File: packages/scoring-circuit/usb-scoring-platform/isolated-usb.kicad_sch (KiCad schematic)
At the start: 10 parts, among them U18 ADuM3160BRWZ

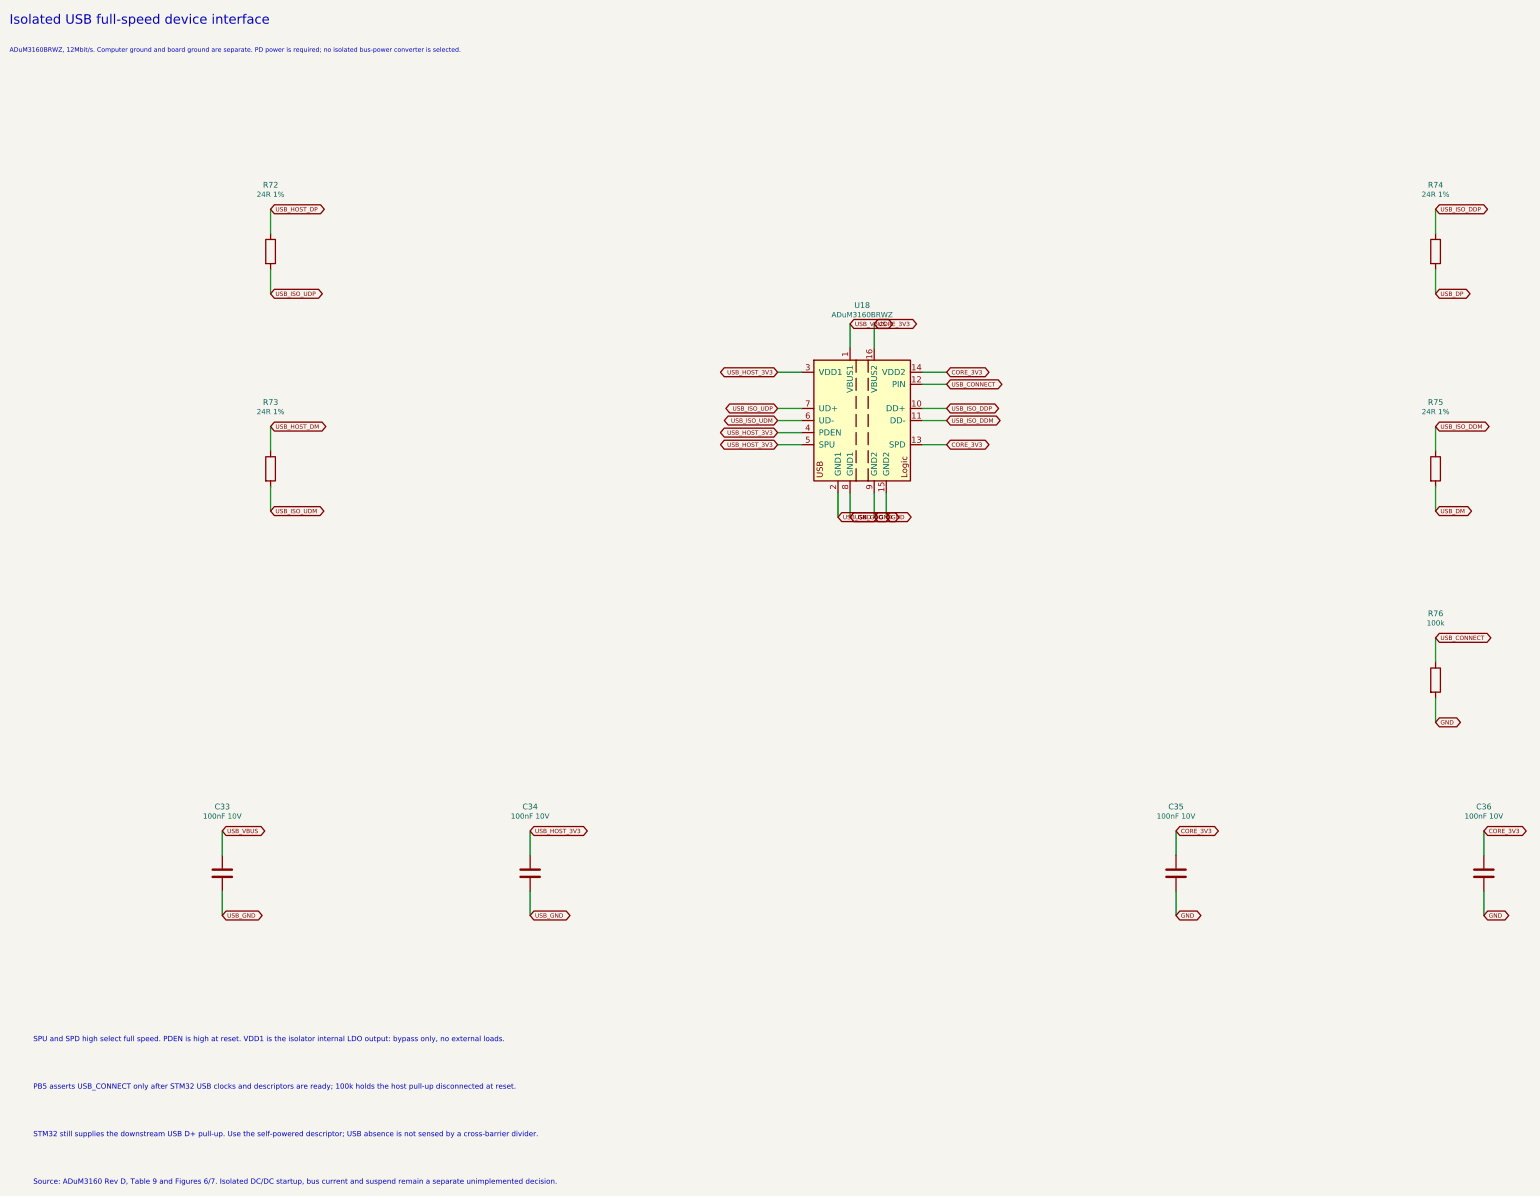
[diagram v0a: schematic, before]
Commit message: feat(scoring-circuit): add isolated single-cable USB acquisition power
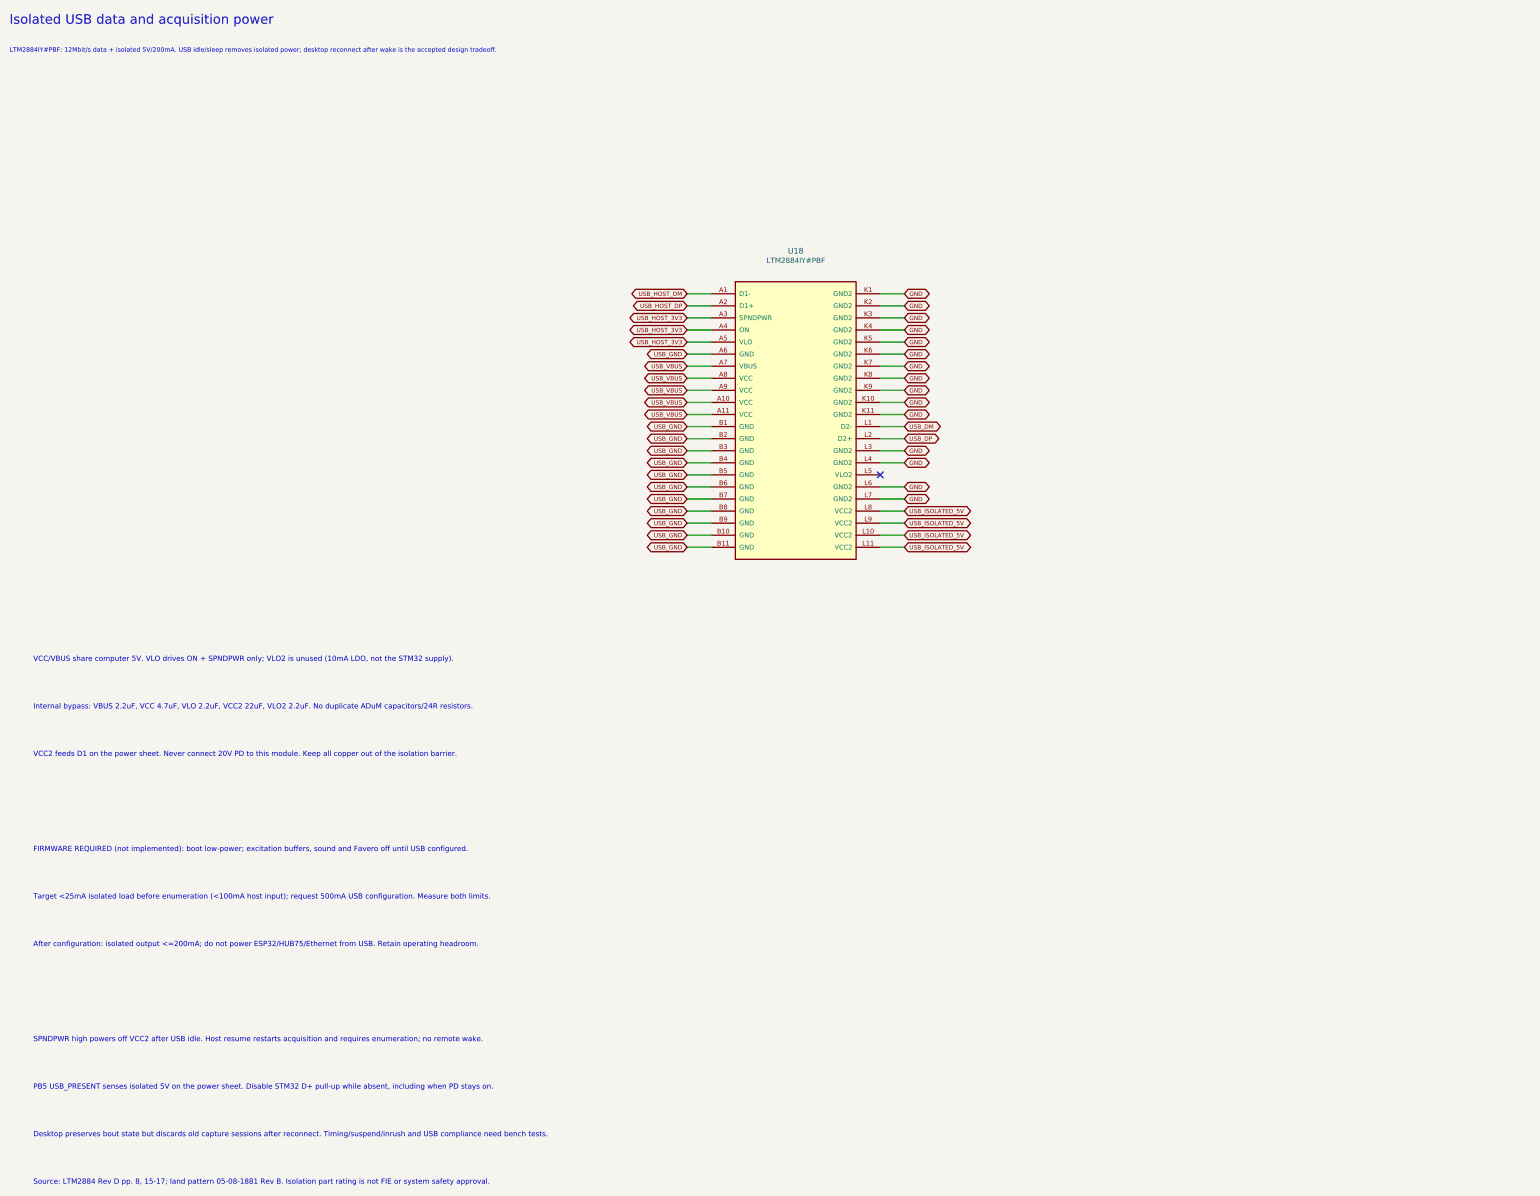
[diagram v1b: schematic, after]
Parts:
- removed C33, C34, C35, C36: 100nF 10V, Capacitor_SMD:C_0603_1608Metric, symbol Device:C
- removed R72, R73, R74, R75: 24R 1%, Resistor_SMD:R_0603_1608Metric, symbol Device:R
- removed R76: 100k, Resistor_SMD:R_0603_1608Metric, symbol Device:R
- U18: value ADuM3160BRWZ -> LTM2884IY#PBF; footprint Package_SO:SOIC-16W_7.5x10.3mm_P1.27mm -> ScoringPlatform:LTM2884_BGA; symbol Interface_USB:ADUM3160 -> ScoringPlatform:LTM2884
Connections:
- net GND: now also U18.K1 (GND2), U18.K10 (GND2), U18.K11 (GND2), U18.K2 (GND2), U18.K3 (GND2), U18.K4 (GND2), U18.K5 (GND2), U18.K6 (GND2), U18.K7 (GND2), U18.K8 (GND2), U18.K9 (GND2), U18.L3 (GND2), U18.L4 (GND2), U18.L6 (GND2), U18.L7 (GND2); no longer U18.15 (GND2), U18.9 (GND2)
- net USB_DM: now also U18.L1 (D2-)
- net USB_DP: now also U18.L2 (D2+)
- net USB_GND: now also U18.A6 (GND), U18.B1 (GND), U18.B10 (GND), U18.B11 (GND), U18.B2 (GND), U18.B3 (GND), U18.B4 (GND), U18.B5 (GND), U18.B6 (GND), U18.B7 (GND), U18.B8 (GND), U18.B9 (GND); no longer U18.2 (GND1), U18.8 (GND1)
- net USB_HOST_3V3: now also U18.A3 (SPNDPWR), U18.A4 (ON), U18.A5 (VLO); no longer U18.3 (VDD1), U18.4 (PDEN), U18.5 (SPU)
- net USB_HOST_DM: now also U18.A1 (D1-)
- net USB_HOST_DP: now also U18.A2 (D1+)
- net USB_VBUS: now also U18.A10 (VCC), U18.A11 (VCC), U18.A7 (VBUS), U18.A8 (VCC), U18.A9 (VCC); no longer U18.1 (VBUS1)
- removed net CORE_3V3: U18.13 (SPD), U18.14 (VDD2), U18.16 (VBUS2)
- removed net USB_CONNECT: U18.12 (PIN)
- removed net USB_ISO_DDM: U18.11 (DD-)
- removed net USB_ISO_DDP: U18.10 (DD+)
- removed net USB_ISO_UDM: U18.6 (UD-)
- removed net USB_ISO_UDP: U18.7 (UD+)
- new net USB_ISOLATED_5V: U18.L10 (VCC2), U18.L11 (VCC2), U18.L8 (VCC2), U18.L9 (VCC2)
- no-connect marks 0 -> 1
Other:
- note added: "After configuration: isolated output <=200mA; do not power ESP32/HUB75/Ethernet from USB. Retain operating headroom."
- note added: "Desktop preserves bout state but discards old capture sessions after reconnect. Timing/suspend/inrush and USB compliance need bench tests."
- note added: "FIRMWARE REQUIRED (not implemented): boot low-power; excitation buffers, sound and Favero off until USB configured."
- note added: "Internal bypass: VBUS 2.2uF, VCC 4.7uF, VLO 2.2uF, VCC2 22uF, VLO2 2.2uF. No duplicate ADuM capacitors/24R resistors."
- note added: "Isolated USB data and acquisition power"
- note added: "LTM2884IY#PBF: 12Mbit/s data + isolated 5V/200mA. USB idle/sleep removes isolated power; desktop reconnect after wake is the accepted design tradeoff."
- note added: "PB5 USB_PRESENT senses isolated 5V on the power sheet. Disable STM32 D+ pull-up while absent, including when PD stays on."
- note added: "SPNDPWR high powers off VCC2 after USB idle. Host resume restarts acquisition and requires enumeration; no remote wake."
- note added: "Source: LTM2884 Rev D pp. 8, 15-17; land pattern 05-08-1881 Rev B. Isolation part rating is not FIE or system safety approval."
- note added: "Target <25mA isolated load before enumeration (<100mA host input); request 500mA USB configuration. Measure both limits."
- note added: "VCC/VBUS share computer 5V. VLO drives ON + SPNDPWR only; VLO2 is unused (10mA LDO, not the STM32 supply)."
- note added: "VCC2 feeds D1 on the power sheet. Never connect 20V PD to this module. Keep all copper out of the isolation barrier."
- note removed: "ADuM3160BRWZ, 12Mbit/s. Computer ground and board ground are separate. PD power is required; no isolated bus-power converter is selected."
- note removed: "Isolated USB full-speed device interface"
- note removed: "PB5 asserts USB_CONNECT only after STM32 USB clocks and descriptors are ready; 100k holds the host pull-up disconnected at reset."
- note removed: "SPU and SPD high select full speed. PDEN is high at reset. VDD1 is the isolator internal LDO output: bypass only, no external loads."
- note removed: "STM32 still supplies the downstream USB D+ pull-up. Use the self-powered descriptor; USB absence is not sensed by a cross-barrier divider."
- note removed: "Source: ADuM3160 Rev D, Table 9 and Figures 6/7. Isolated DC/DC startup, bus current and suspend remain a separate unimplemented decision."
- title: Isolated USB full-speed device interface -> Isolated USB data and acquisition power

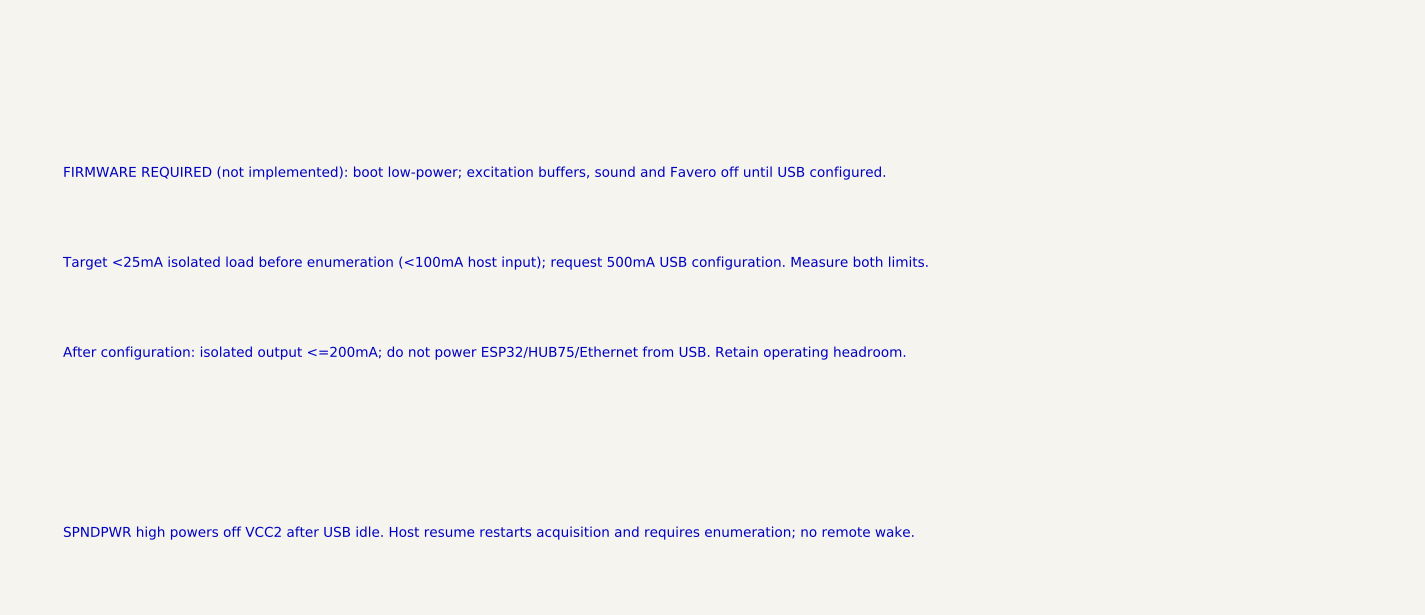
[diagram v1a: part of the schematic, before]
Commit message: docs(scoring-circuit): bound laptop acquisition power
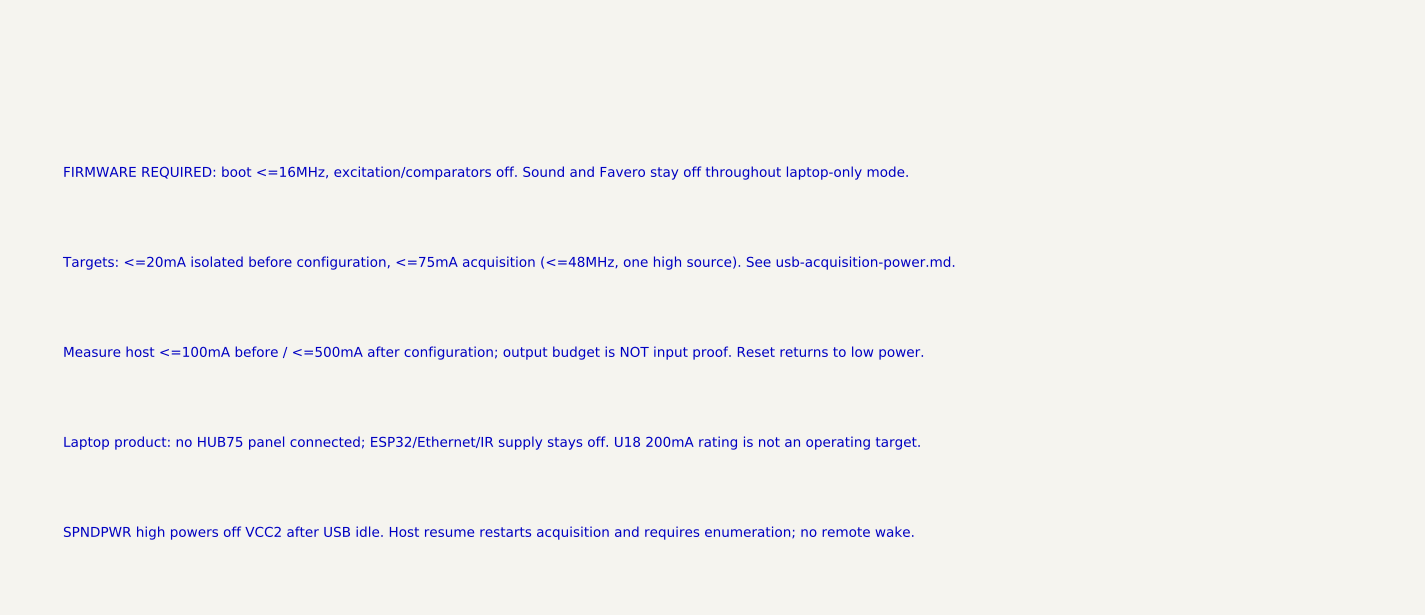
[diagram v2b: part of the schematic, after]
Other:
- note added: "FIRMWARE REQUIRED: boot <=16MHz, excitation/comparators off. Sound and Favero stay off throughout laptop-only mode."
- note added: "Laptop product: no HUB75 panel connected; ESP32/Ethernet/IR supply stays off. U18 200mA rating is not an operating target."
- note added: "Measure host <=100mA before / <=500mA after configuration; output budget is NOT input proof. Reset returns to low power."
- note added: "Targets: <=20mA isolated before configuration, <=75mA acquisition (<=48MHz, one high source). See usb-acquisition-power.md."
- note removed: "After configuration: isolated output <=200mA; do not power ESP32/HUB75/Ethernet from USB. Retain operating headroom."
- note removed: "FIRMWARE REQUIRED (not implemented): boot low-power; excitation buffers, sound and Favero off until USB configured."
- note removed: "Target <25mA isolated load before enumeration (<100mA host input); request 500mA USB configuration. Measure both limits."

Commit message: feat(scoring-circuit): replace dual USB inputs with shared isolated power design
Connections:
- net USB_VBUS renamed USB_PRIMARY_5V

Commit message: chore(scoring-circuit): complete assembly BOM ordering fields
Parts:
- U18: MPN (none) -> LTM2884IY#PBF; Manufacturer (none) -> Analog Devices
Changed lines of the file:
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@@
 (paper "A3")
 (title_block (title "Isolated USB data and acquisition power") (rev "Engineering draft") (comment 1 "NOT FOR FABRICATION"))
-(symbol (lib_id "ScoringPlatform:LTM2884") (at 185.42 100.33 0) (unit 1) (in_bom yes) (on_board yes) (dnp no) (property "Reference" "U18" (at 185.42 64.66 0) (effects (font (size 1.2 1.2)))) (property "Value" "LTM2884IY#PBF" (at 185.42 66.66 0) (effects (font (size 1.1 1.1)))) (property "Footprint" "ScoringPlatform:LTM2884_BGA" (at 185.42 100.33 0) (effects (font (size 1 1)) (hide yes))) (pin "A1") (pin "A2") (pin "A3") (pin "A4") (pin "A5") (pin "A6") (pin "A7") (pin "A8") (pin "A9") (pin "A10") (pin "A11") (pin "B1") (pin "B2") (pin "B3") (pin "B4") (pin "B5") (pin "B6") (pin "B7") (pin "B8") (pin "B9") (pin "B10") (pin "B11") (pin "K1") (pin "K2") (pin "K3") (pin "K4") (pin "K5") (pin "K6") (pin "K7") (pin "K8") (pin "K9") (pin "K10") (pin "K11") (pin "L1") (pin "L2") (pin "L3") (pin "L4") (pin "L5") (pin "L6") (pin "L7") (pin "L8") (pin "L9") (pin "L10") (pin "L11") (property "Datasheet" "https://www.analog.com/media/en/technical-documentation/data-sheets/ltm2884.pdf" (at 185.42 100.33 0) (effects (font (size 1 1)) (hide yes))) (instances (project "usb-scoring-platform" (path "/20cc8167-128c-446a-a106-f942323e143f/e55d854e-24ef-4e48-a304-9dbb04dce049" (reference "U18") (unit 1)))))
+(symbol (lib_id "ScoringPlatform:LTM2884") (at 185.42 100.33 0) (unit 1) (in_bom yes) (on_board yes) (dnp no) (property "Reference" "U18" (at 185.42 64.66 0) (effects (font (size 1.2 1.2)))) (property "Value" "LTM2884IY#PBF" (at 185.42 66.66 0) (effects (font (size 1.1 1.1)))) (property "Footprint" "ScoringPlatform:LTM2884_BGA" (at 185.42 100.33 0) (effects (font (size 1 1)) (hide yes))) (pin "A1") (pin "A2") (pin "A3") (pin "A4") (pin "A5") (pin "A6") (pin "A7") (pin "A8") (pin "A9") (pin "A10") (pin "A11") (pin "B1") (pin "B2") (pin "B3") (pin "B4") (pin "B5") (pin "B6") (pin "B7") (pin "B8") (pin "B9") (pin "B10") (pin "B11") (pin "K1") (pin "K2") (pin "K3") (pin "K4") (pin "K5") (pin "K6") (pin "K7") (pin "K8") (pin "K9") (pin "K10") (pin "K11") (pin "L1") (pin "L2") (pin "L3") (pin "L4") (pin "L5") (pin "L6") (pin "L7") (pin "L8") (pin "L9") (pin "L10") (pin "L11") (property "Datasheet" "https://www.analog.com/media/en/technical-documentation/data-sheets/ltm2884.pdf" (at 185.42 100.33 0) (effects (font (size 1 1)) (hide yes))) (instances (project "usb-scoring-platform" (path "/20cc8167-128c-446a-a106-f942323e143f/e55d854e-24ef-4e48-a304-9dbb04dce049" (reference "U18") (unit 1)))) (property "Manufacturer" "Analog Devices" (at 0 0 0) (effects (font (size 1 1)) (hide yes))) (property "MPN" "LTM2884IY#PBF" (at 0 0 0) (effects (font (size 1 1)) (hide yes))))
 (wire (pts (xy 167.64 73.66) (xy 162.56 73.66)) (stroke (width 0) (type default)))
 (global_label "USB_HOST_DM" (shape bidirectional) (at 162.56 73.66 180) (effects (font (size 0.9 0.9)) (justify right)) (property "Intersheetrefs" "" (at 162.56 73.66 180) (effects (font (size 1 1)) (hide yes))))
